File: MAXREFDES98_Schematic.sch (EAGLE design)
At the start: 15 parts, among them T1 TG110-S055N2RL

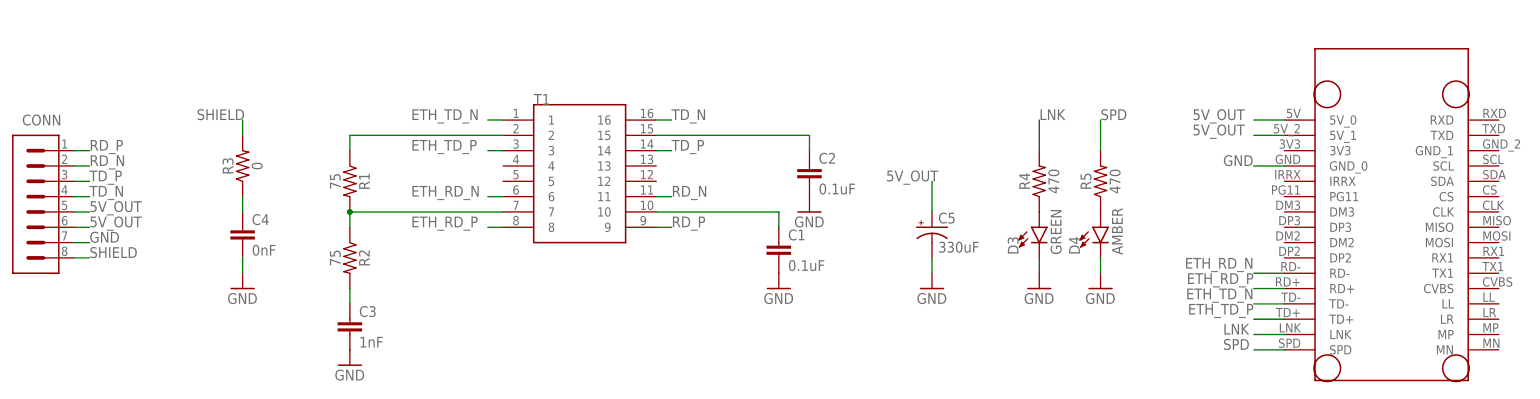
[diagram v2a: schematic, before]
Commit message: Added schematic labels, 1206 cap, fixed ethernet line width
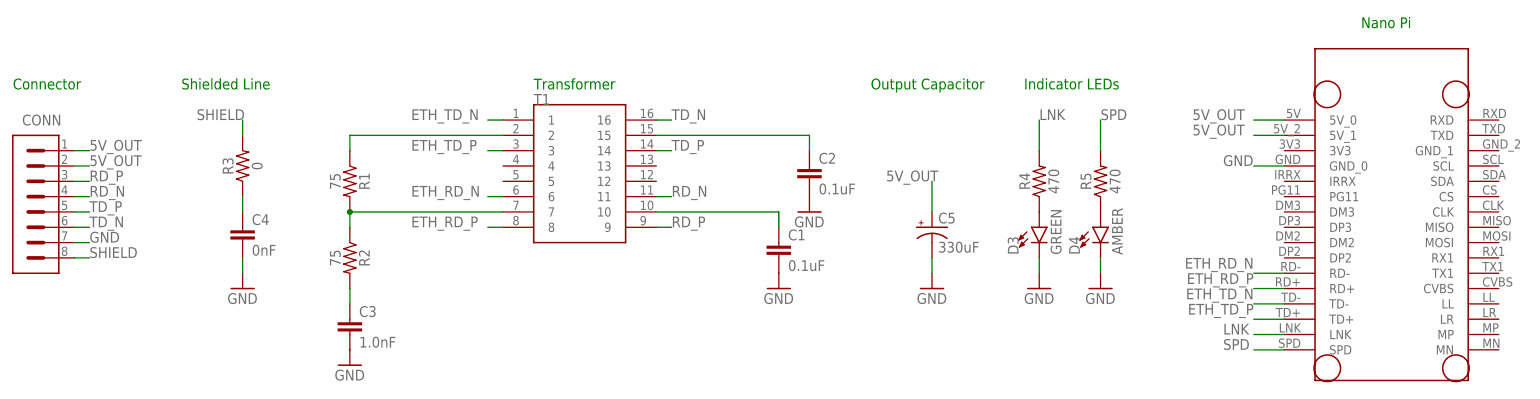
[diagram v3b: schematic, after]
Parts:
- C3: value 1nF -> 1.0nF; device SparkFun-Capacitors:1.0NF/1000PF-0603-50V-10% -> SparkFun-Capacitors:1.0UF-1206-50V-10%
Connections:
- net 5V_OUT: now also CONN.1, CONN.2; no longer CONN.5, CONN.6
- net RD_N: now also CONN.4; no longer CONN.2
- net RD_P: now also CONN.3; no longer CONN.1
- net TD_N: now also CONN.6; no longer CONN.4
- net TD_P: now also CONN.5; no longer CONN.3
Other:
- note added: "Connector"
- note added: "Indicator LEDs"
- note added: "Nano Pi"
- note added: "Output Capacitor"
- note added: "Shielded Line"
- note added: "Transformer"
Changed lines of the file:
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@@
 <part name="C1" library="SparkFun-Capacitors" library_urn="urn:adsk.eagle:library:510" deviceset="0.1UF" device="-0603-25V-(+80/-20%)" package3d_urn="urn:adsk.eagle:package:37414/1" value="0.1uF"/>
 <part name="C2" library="SparkFun-Capacitors" library_urn="urn:adsk.eagle:library:510" deviceset="0.1UF" device="-0603-25V-(+80/-20%)" package3d_urn="urn:adsk.eagle:package:37414/1" value="0.1uF"/>
-<part name="C3" library="SparkFun-Capacitors" library_urn="urn:adsk.eagle:library:510" deviceset="1.0NF/1000PF" device="-0603-50V-10%" package3d_urn="urn:adsk.eagle:package:37414/1" value="1nF"/>
 <part name="GND1" library="supply1" library_urn="urn:adsk.eagle:library:371" deviceset="GND" device=""/>
 <part name="GND6" library="supply1" library_urn="urn:adsk.eagle:library:371" deviceset="GND" device=""/>
@@
 <part name="C4" library="SparkFun-Capacitors" library_urn="urn:adsk.eagle:library:510" deviceset="3.3NF" device="-0603-100V-10%" package3d_urn="urn:adsk.eagle:package:37414/1" value="0nF"/>
 <part name="GND5" library="supply1" library_urn="urn:adsk.eagle:library:371" deviceset="GND" device=""/>
+<part name="C3" library="SparkFun-Capacitors" library_urn="urn:adsk.eagle:library:510" deviceset="1.0UF" device="-1206-50V-10%" package3d_urn="urn:adsk.eagle:package:37426/1" value="1.0nF"/>
 </parts>
 <sheets>
 <sheet>
 <plain>
+<text x="12.7" y="76.2" size="1.778" layer="91">Connector</text>
+<text x="40.64" y="76.2" size="1.778" layer="91">Shielded Line</text>
+<text x="99.06" y="76.2" size="1.778" layer="91">Transformer</text>
+<text x="154.94" y="76.2" size="1.778" layer="91">Output Capacitor</text>
+<text x="180.34" y="76.2" size="1.778" layer="91">Indicator LEDs</text>
+<text x="236.22" y="86.36" size="1.778" layer="91">Nano Pi</text>
 </plain>
 <instances>
@@
 <attribute name="VALUE" x="146.304" y="58.801" size="1.778" layer="96" font="vector"/>
 </instance>
+<instance part="GND1" gate="1" x="139.7" y="43.18" smashed="yes">
+<attribute name="VALUE" x="137.16" y="40.64" size="1.778" layer="96"/>
+</instance>
+<instance part="GND6" gate="1" x="144.78" y="55.88" smashed="yes">
+<attribute name="VALUE" x="142.24" y="53.34" size="1.778" layer="96"/>
+</instance>
+<instance part="R1" gate="G$1" x="68.58" y="60.96" smashed="yes" rot="R270">
+<attribute name="NAME" x="70.104" y="60.96" size="1.778" layer="95" font="vector" rot="R270" align="bottom-center"/>
+<attribute name="VALUE" x="67.056" y="60.96" size="1.778" layer="96" font="vector" rot="R270" align="top-center"/>
+</instance>
+<instance part="R2" gate="G$1" x="68.58" y="48.26" smashed="yes" rot="R270">
+<attribute name="NAME" x="70.104" y="48.26" size="1.778" layer="95" font="vector" rot="R270" align="bottom-center"/>
+<attribute name="VALUE" x="67.056" y="48.26" size="1.778" layer="96" font="vector" rot="R270" align="top-center"/>
+</instance>
+<instance part="GND7" gate="1" x="68.58" y="30.48" smashed="yes">
+<attribute name="VALUE" x="66.04" y="27.94" size="1.778" layer="96"/>
+</instance>
+<instance part="R3" gate="G$1" x="50.8" y="63.5" smashed="yes" rot="R90">
+<attribute name="NAME" x="49.276" y="63.5" size="1.778" layer="95" font="vector" rot="R90" align="bottom-center"/>
+<attribute name="VALUE" x="52.324" y="63.5" size="1.778" layer="96" font="vector" rot="R90" align="top-center"/>
+</instance>
+<instance part="C4" gate="G$1" x="50.8" y="50.8" smashed="yes">
+<attribute name="NAME" x="52.324" y="53.721" size="1.778" layer="95" font="vector"/>
+<attribute name="VALUE" x="52.324" y="48.641" size="1.778" layer="96" font="vector"/>
+</instance>
+<instance part="GND5" gate="1" x="50.8" y="43.18" smashed="yes">
+<attribute name="VALUE" x="48.26" y="40.64" size="1.778" layer="96"/>
+</instance>
 <instance part="C3" gate="G$1" x="68.58" y="35.56" smashed="yes">
 <attribute name="NAME" x="70.104" y="38.481" size="1.778" layer="95" font="vector"/>
 <attribute name="VALUE" x="70.104" y="33.401" size="1.778" layer="96" font="vector"/>
-</instance>
-<instance part="GND1" gate="1" x="139.7" y="43.18" smashed="yes">
-<attribute name="VALUE" x="137.16" y="40.64" size="1.778" layer="96"/>
-</instance>
-<instance part="GND6" gate="1" x="144.78" y="55.88" smashed="yes">
-<attribute name="VALUE" x="142.24" y="53.34" size="1.778" layer="96"/>
-</instance>
-<instance part="R1" gate="G$1" x="68.58" y="60.96" smashed="yes" rot="R270">
-<attribute name="NAME" x="70.104" y="60.96" size="1.778" layer="95" font="vector" rot="R270" align="bottom-center"/>
-<attribute name="VALUE" x="67.056" y="60.96" size="1.778" layer="96" font="vector" rot="R270" align="top-center"/>
-</instance>
-<instance part="R2" gate="G$1" x="68.58" y="48.26" smashed="yes" rot="R270">
-<attribute name="NAME" x="70.104" y="48.26" size="1.778" layer="95" font="vector" rot="R270" align="bottom-center"/>
-<attribute name="VALUE" x="67.056" y="48.26" size="1.778" layer="96" font="vector" rot="R270" align="top-center"/>
-</instance>
-<instance part="GND7" gate="1" x="68.58" y="30.48" smashed="yes">
-<attribute name="VALUE" x="66.04" y="27.94" size="1.778" layer="96"/>
-</instance>
-<instance part="R3" gate="G$1" x="50.8" y="63.5" smashed="yes" rot="R90">
-<attribute name="NAME" x="49.276" y="63.5" size="1.778" layer="95" font="vector" rot="R90" align="bottom-center"/>
-<attribute name="VALUE" x="52.324" y="63.5" size="1.778" layer="96" font="vector" rot="R90" align="top-center"/>
-</instance>
-<instance part="C4" gate="G$1" x="50.8" y="50.8" smashed="yes">
-<attribute name="NAME" x="52.324" y="53.721" size="1.778" layer="95" font="vector"/>
-<attribute name="VALUE" x="52.324" y="48.641" size="1.778" layer="96" font="vector"/>
-</instance>
-<instance part="GND5" gate="1" x="50.8" y="43.18" smashed="yes">
-<attribute name="VALUE" x="48.26" y="40.64" size="1.778" layer="96"/>
 </instance>
 </instances>
@@
 </segment>
 <segment>
-<wire x1="22.86" y1="55.88" x2="25.4" y2="55.88" width="0.1524" layer="91"/>
-<pinref part="CONN" gate="G$1" pin="5"/>
-<label x="25.4" y="55.88" size="1.778" layer="95"/>
-</segment>
-<segment>
-<wire x1="22.86" y1="53.34" x2="25.4" y2="53.34" width="0.1524" layer="91"/>
-<pinref part="CONN" gate="G$1" pin="6"/>
-<label x="25.4" y="53.34" size="1.778" layer="95"/>
-</segment>
-<segment>
 <pinref part="C5" gate="G$1" pin="+"/>
 <wire x1="165.1" y1="55.88" x2="165.1" y2="60.96" width="0.1524" layer="91"/>
 <label x="157.48" y="60.96" size="1.778" layer="95"/>
 </segment>
+<segment>
+<pinref part="CONN" gate="G$1" pin="1"/>
+<wire x1="22.86" y1="66.04" x2="25.4" y2="66.04" width="0.1524" layer="91"/>
+<label x="25.4" y="66.04" size="1.778" layer="95"/>
+</segment>
+<segment>
+<pinref part="CONN" gate="G$1" pin="2"/>
+<wire x1="22.86" y1="63.5" x2="25.4" y2="63.5" width="0.1524" layer="91"/>
+<label x="25.4" y="63.5" size="1.778" layer="95"/>
+</segment>
 </net>
 <net name="GND" class="0">
@@
 </segment>
 <segment>
-<pinref part="GND7" gate="1" pin="GND"/>
-<pinref part="C3" gate="G$1" pin="2"/>
-</segment>
-<segment>
 <wire x1="22.86" y1="50.8" x2="25.4" y2="50.8" width="0.1524" layer="91"/>
 <pinref part="CONN" gate="G$1" pin="7"/>
@@
 <wire x1="50.8" y1="48.26" x2="50.8" y2="45.72" width="0.1524" layer="91"/>
 </segment>
+<segment>
+<pinref part="GND7" gate="1" pin="GND"/>
+<pinref part="C3" gate="G$1" pin="2"/>
+</segment>
 </net>
 <net name="SHIELD" class="0">
@@
 </segment>
 <segment>
-<pinref part="CONN" gate="G$1" pin="2"/>
-<wire x1="22.86" y1="63.5" x2="25.4" y2="63.5" width="0.1524" layer="91"/>
-<label x="25.4" y="63.5" size="1.778" layer="95"/>
+<pinref part="CONN" gate="G$1" pin="4"/>
+<wire x1="22.86" y1="58.42" x2="25.4" y2="58.42" width="0.1524" layer="91"/>
+<label x="25.4" y="58.42" size="1.778" layer="95"/>
 </segment>
 </net>
@@
 </segment>
 <segment>
-<wire x1="22.86" y1="66.04" x2="25.4" y2="66.04" width="0.1524" layer="91"/>
-<pinref part="CONN" gate="G$1" pin="1"/>
-<label x="25.4" y="66.04" size="1.778" layer="95"/>
+<pinref part="CONN" gate="G$1" pin="3"/>
+<wire x1="22.86" y1="60.96" x2="25.4" y2="60.96" width="0.1524" layer="91"/>
+<label x="25.4" y="60.96" size="1.778" layer="95"/>
 </segment>
 </net>
@@
 </segment>
 <segment>
-<wire x1="22.86" y1="58.42" x2="25.4" y2="58.42" width="0.1524" layer="91"/>
-<pinref part="CONN" gate="G$1" pin="4"/>
-<label x="25.4" y="58.42" size="1.778" layer="95"/>
+<pinref part="CONN" gate="G$1" pin="6"/>
+<wire x1="22.86" y1="53.34" x2="25.4" y2="53.34" width="0.1524" layer="91"/>
+<label x="25.4" y="53.34" size="1.778" layer="95"/>
 </segment>
 </net>
@@
 </segment>
 <segment>
-<wire x1="22.86" y1="60.96" x2="25.4" y2="60.96" width="0.1524" layer="91"/>
-<pinref part="CONN" gate="G$1" pin="3"/>
-<label x="25.4" y="60.96" size="1.778" layer="95"/>
-</segment>
-</net>
+<pinref part="CONN" gate="G$1" pin="5"/>
+<wire x1="22.86" y1="55.88" x2="25.4" y2="55.88" width="0.1524" layer="91"/>
+<label x="25.4" y="55.88" size="1.778" layer="95"/>
+</segment>
+</net>

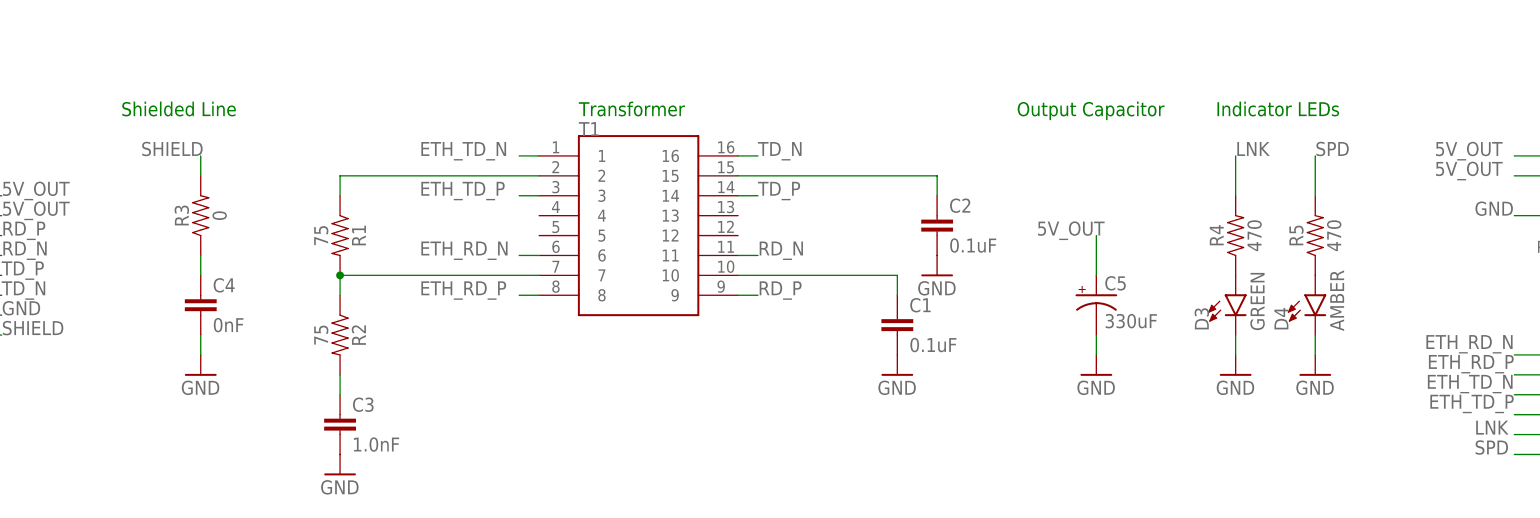
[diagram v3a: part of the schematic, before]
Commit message: Added Power Indicator LED, shortened board
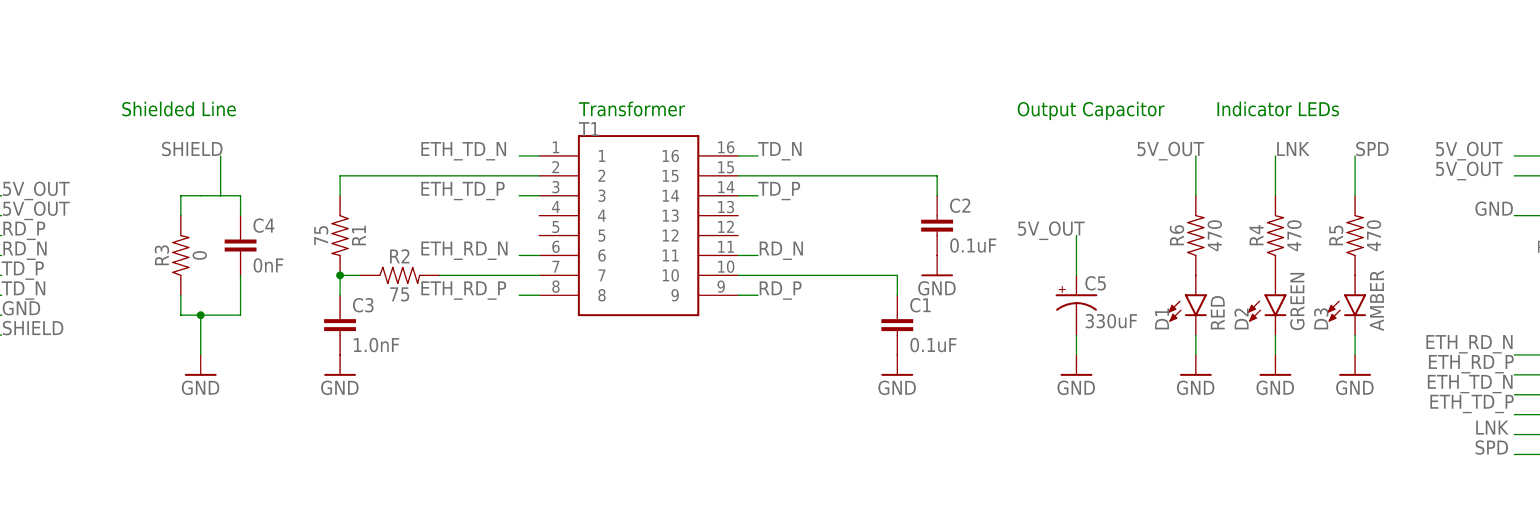
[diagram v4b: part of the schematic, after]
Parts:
- removed D4: AMBER, SparkFun-LED:LED-FKIT-1206
- added D1: RED, SparkFun-LED:LED-FKIT-1206
- added D2: GREEN, SparkFun-LED:LED-FKIT-1206
- added R6: 470, SparkFun-Resistors:0OHM-0603-1/10W-5%
- D3: value GREEN -> AMBER
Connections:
- removed net N$14: R1.2, R2.1, T1.7
- new net N$5: D1.A, R6.1
- net 5V_OUT: now also R6.2
- net GND: now also D1.C, D2.C, R3.1; no longer D4.C
- net N$1: now also D2.A; no longer D3.A
- net N$2: now also D3.A; no longer D4.A
- net N$3: now also T1.7; no longer C3.1
- net N$4: now also C3.1, R1.2, R2.1; no longer C4.1, R3.1
- net SHIELD: now also C4.1
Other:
- moved on the sheet: C3, C4, C5, D3, R2, R3, R4, R5
